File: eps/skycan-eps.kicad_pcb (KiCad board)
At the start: 2 copper layers, 50 x 50 mm, 43 parts, among them J1 DF9-25P-1V-PLUG, J2 DF9-25P-1V-SOCKET, J3 DF9-25P-1V-PLUG, J4 DF9-25P-1V-SOCKET, U1 TPS63060, U2 BQ27210, U3 MICRO-B_USB, U4 MCP73831, U5 SWITCH-DPDT

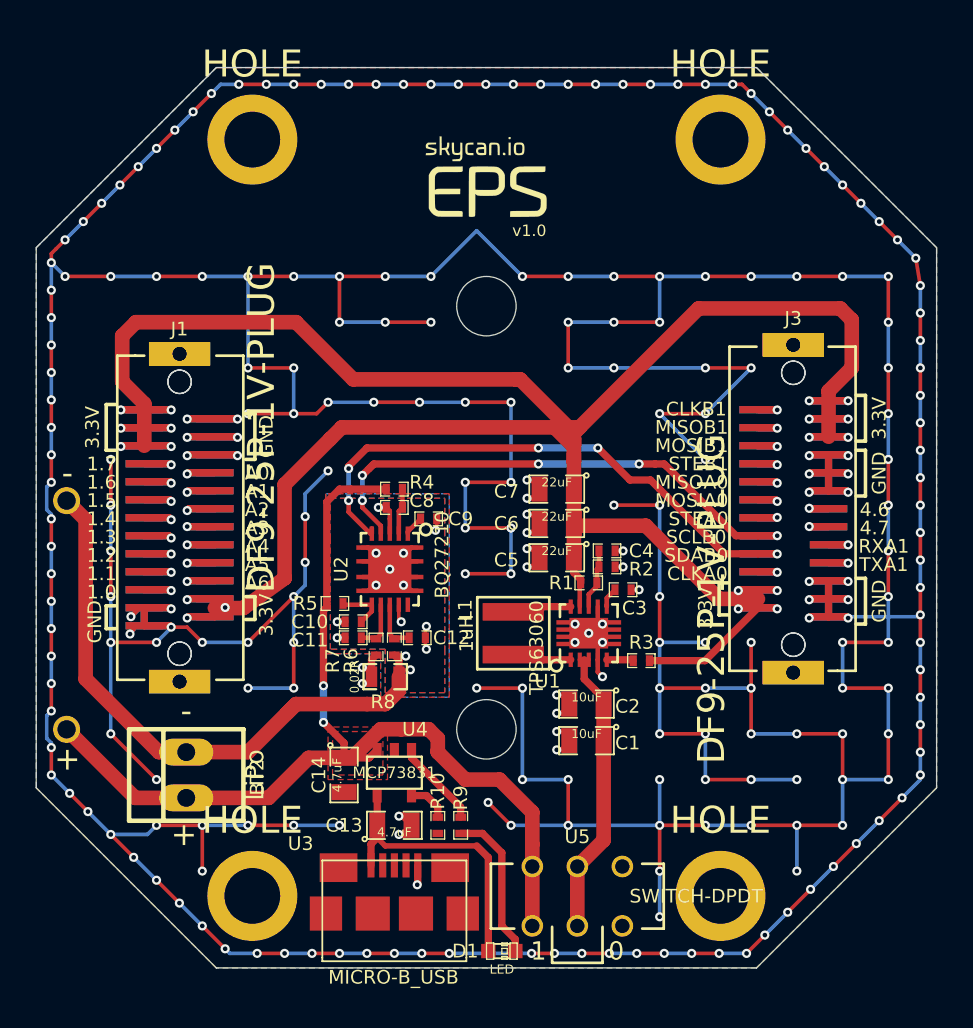
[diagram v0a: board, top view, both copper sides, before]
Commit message: EPS board now uses only skycan lib.
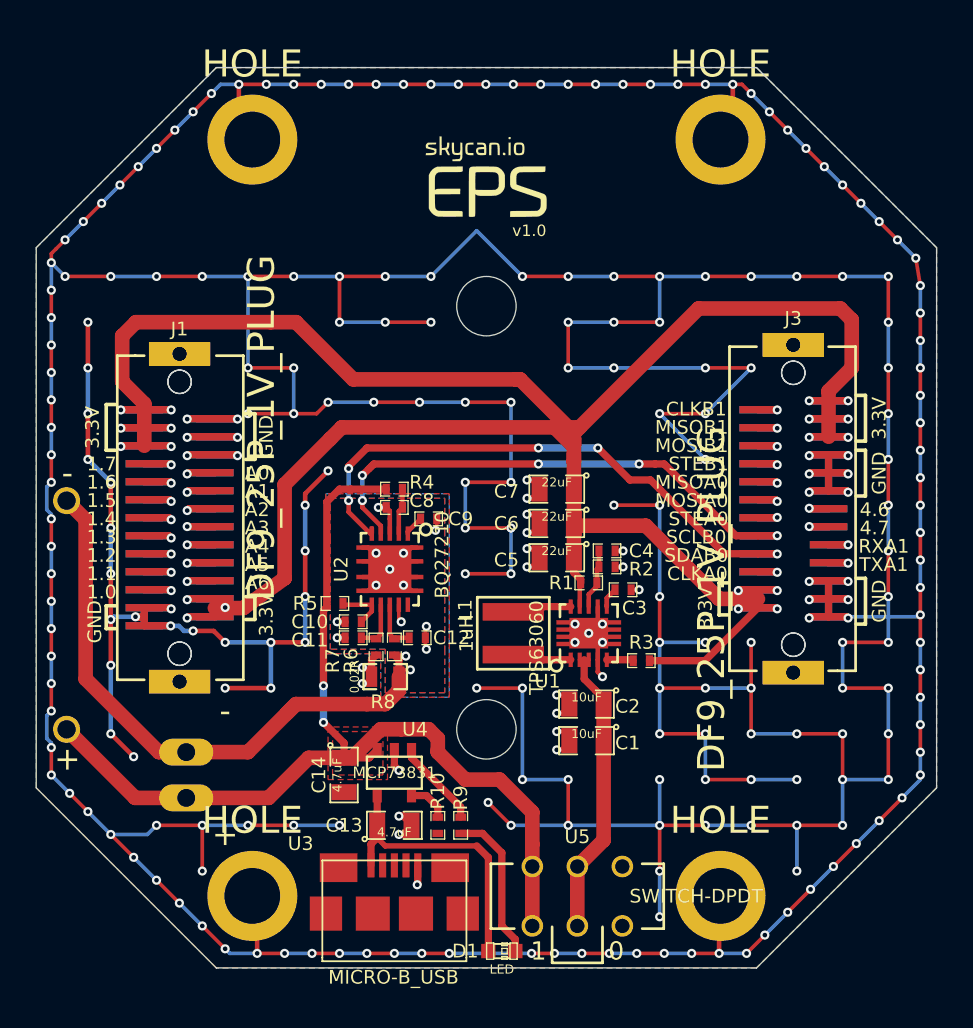
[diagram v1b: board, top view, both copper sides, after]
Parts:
- BT2: moved to B.Cu
- J1, J3: value DF9-25P-1V-PLUG -> DF9_25P_1V_PLUG
- J2, J4: value DF9-25P-1V-SOCKET -> DF9_25P_1V_SOCKET
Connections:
- H1 pad 1: (no net) -> GND
- H2 pad 1: (no net) -> GND
- H3 pad 1: (no net) -> GND
- H4 pad 1: (no net) -> GND
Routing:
- net GND: track 585.4 -> 600.8 mm, vias 270 -> 274
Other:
- rule via_min_size: 0.4064 -> 0.0254

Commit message: Added more vias to EPS pwrgnd plane
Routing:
- net GNDPWR: track 66.5 -> 69.3 mm, vias 14 -> 18
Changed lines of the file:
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@@
     (thickness 1.6)
     (drawings 82)
-    (tracks 1222)
+    (tracks 1234)
     (zones 0)
     (modules 43)
@@
   (segment (start 107.493 120.061) (end 107.432 120) (width 0.4064) (layer B.Cu) (net 13))
   (segment (start 107.432 120) (end 106 120) (width 0.4064) (layer B.Cu) (net 13))
+  (segment (start 121.159 116.656) (end 121.723 116.656) (width 0.1524) (layer F.Cu) (net 14) (status 400000))
+  (via (at 121.793 116.586) (size 0.508) (layers F.Cu B.Cu) (net 14))
+  (segment (start 121.723 116.656) (end 121.793 116.586) (width 0.1524) (layer F.Cu) (net 14))
+  (segment (start 121.159 119.056) (end 121.736 119.056) (width 0.1524) (layer F.Cu) (net 14) (status 400000))
+  (via (at 121.793 118.872) (size 0.508) (layers F.Cu B.Cu) (net 14))
+  (segment (start 121.736 119.056) (end 121.793 118.872) (width 0.1524) (layer F.Cu) (net 14))
+  (segment (start 118.109 119.056) (end 117.659 119.056) (width 0.1524) (layer F.Cu) (net 14))
+  (via (at 117.475 118.872) (size 0.508) (layers F.Cu B.Cu) (net 14))
+  (segment (start 117.659 119.056) (end 117.475 118.872) (width 0.1524) (layer F.Cu) (net 14))
+  (segment (start 118.109 116.656) (end 117.545 116.656) (width 0.1524) (layer F.Cu) (net 14))
+  (via (at 117.475 116.586) (size 0.508) (layers F.Cu B.Cu) (net 14))
+  (segment (start 117.545 116.656) (end 117.475 116.586) (width 0.1524) (layer F.Cu) (net 14))
   (segment (start 108.331 128.016) (end 106.807 128.016) (width 0.8128) (layer F.Cu) (net 14))
   (segment (start 102.743 115.108) (end 101.685 114.05) (width 0.8128) (layer F.Cu) (net 14) (status 20))
